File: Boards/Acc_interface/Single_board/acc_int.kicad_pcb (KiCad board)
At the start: 4 copper layers, 85 x 70 mm, 9 parts, among them J1 Ampseal_23_VT, J2 MM_F_RA_20, J3 MM_F_RA_04, J4 MM_F_RA_14, J5 MM_F_RA_06, J6 MicroFit_RA_10, U1 RJ45_VT, U2 RJ45_VT

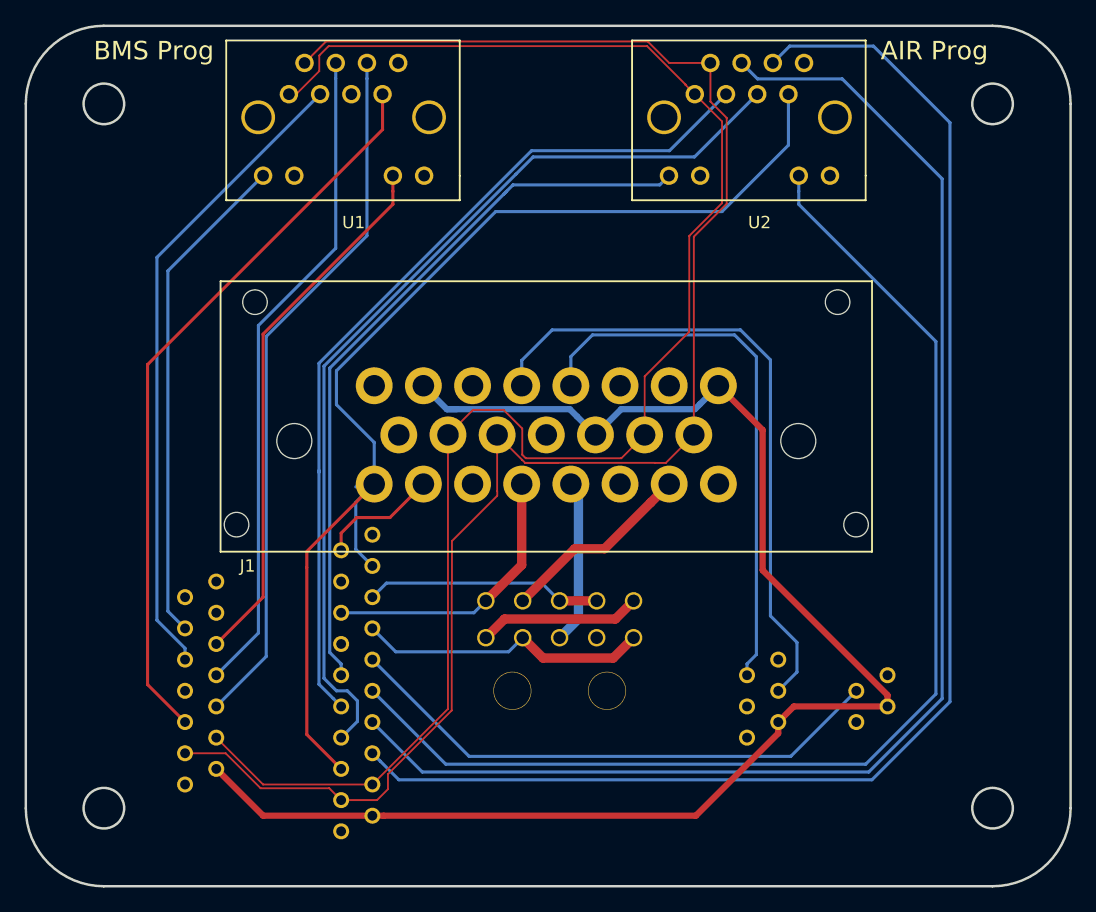
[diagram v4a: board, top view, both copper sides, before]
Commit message: Modified Acc Interface
Fixed micromatch footprints from male to female
Retraced some lines to fit around footprint
updated footprints to match library
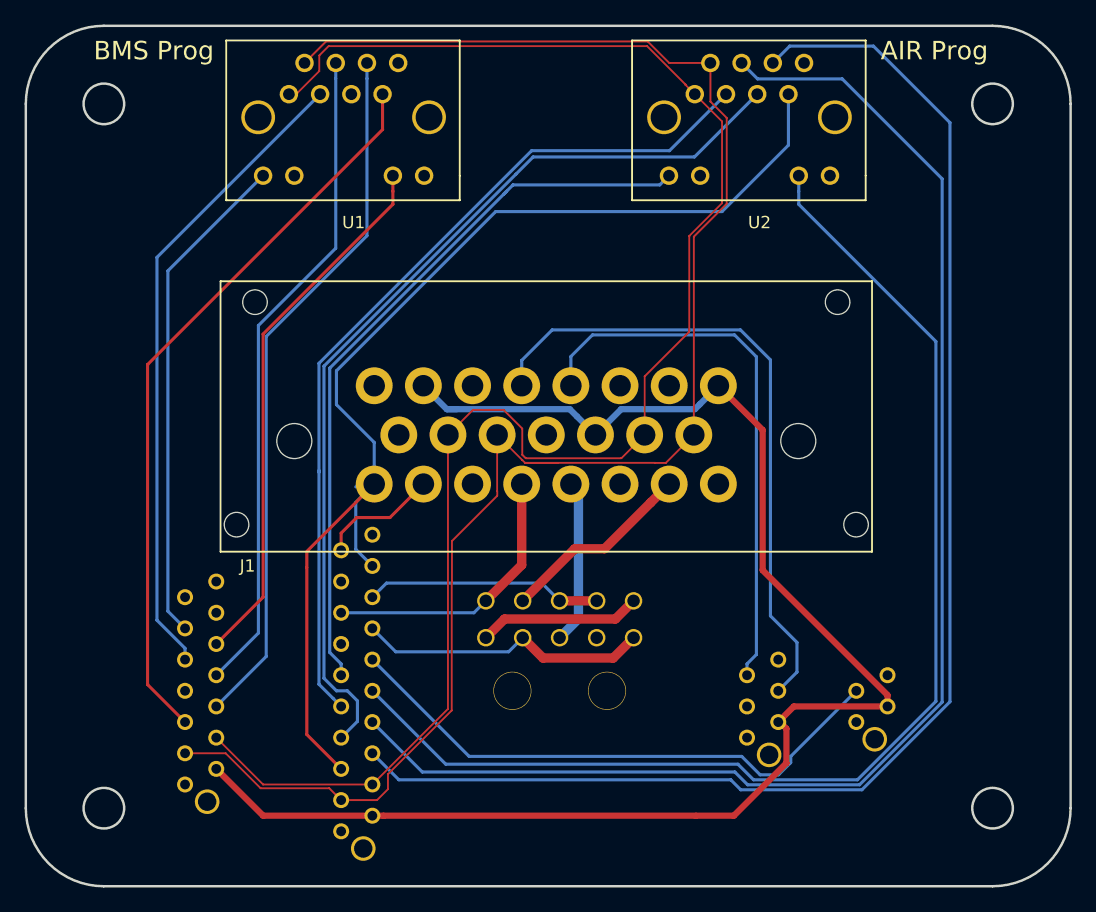
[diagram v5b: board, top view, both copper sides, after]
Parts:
- J2: footprint footprints:micromatch_female_ra_20 -> footprints:micromatch_female_vert_20
- J3: footprint footprints:micromatch_female_ra_4 -> footprints:micromatch_female_vert_4
- J4: footprint footprints:micromatch_female_ra_14 -> footprints:micromatch_female_vert_14
- J5: footprint footprints:micromatch_female_ra_6 -> footprints:micromatch_female_vert_6
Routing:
- net /12V: track 120.3 -> 122.7 mm
- net /IMD_SENSE: track 44.8 -> 46.4 mm
- net /LED1_AIR: track 97.5 -> 98.9 mm
- net /SCK_AIR: track 113.0 -> 114.1 mm
- net /MOSI_AIR: track 115.2 -> 115.9 mm
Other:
- board text removed: "For Instructional Use Only."
- board text removed: "SOLIDWORKS Educational Product."
